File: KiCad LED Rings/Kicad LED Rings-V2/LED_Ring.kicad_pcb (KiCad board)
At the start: 4 copper layers, 30 x 30 mm, 28 parts, among them J1 Conn_01x02_Female, J2 Conn_01x02_Male, U1 LM3509SD_NOPB

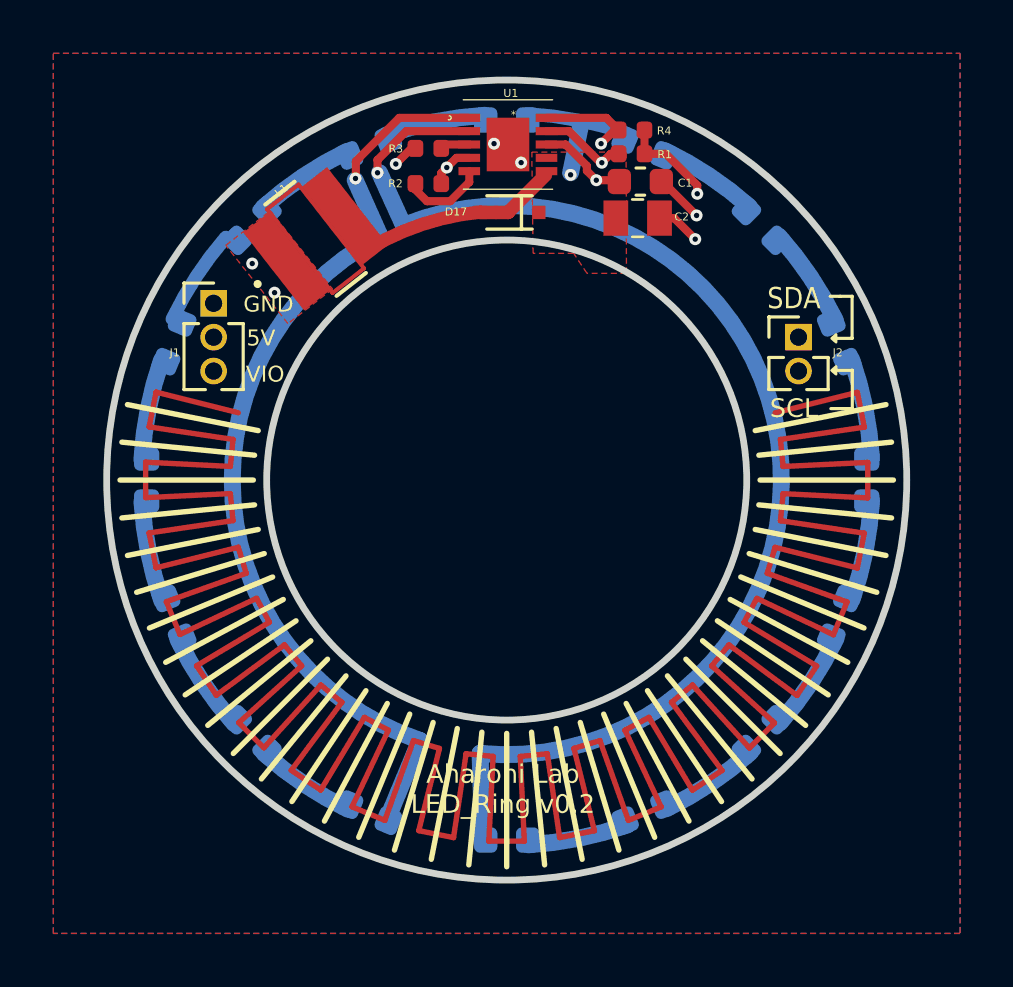
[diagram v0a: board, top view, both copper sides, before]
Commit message: Modified PCB layout
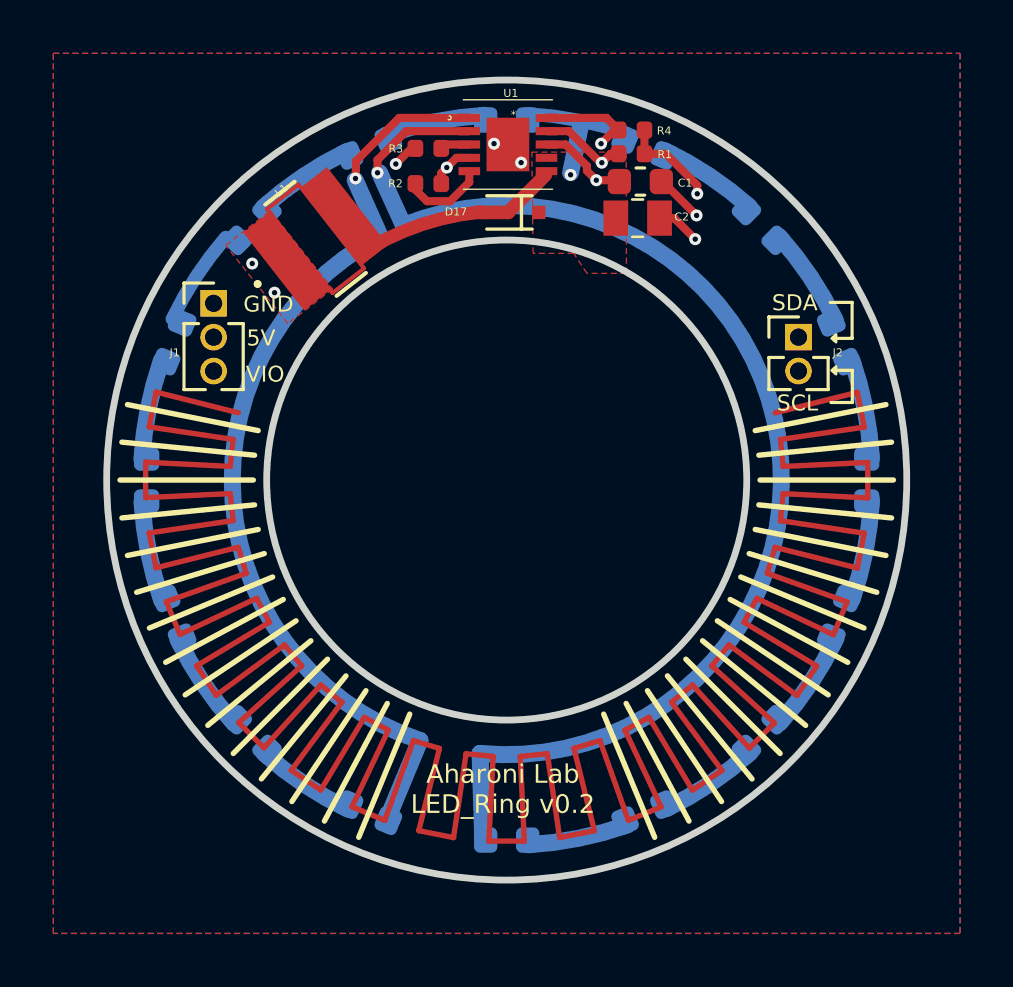
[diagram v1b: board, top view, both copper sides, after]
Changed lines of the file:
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@@
   (general
     (thickness 1.6)
-    (drawings 166)
+    (drawings 159)
     (tracks 105)
     (zones 0)
@@
   (gr_line (start 115.277917 87.898961) (end 118.055768 92.056309) (layer F.SilkS) (width 0.203))
   (gr_line (start 113.635493 88.776856) (end 115.54891 93.396254) (layer F.SilkS) (width 0.203))
-  (gr_line (start 111.853358 89.31746) (end 112.82881 94.221386) (layer F.SilkS) (width 0.203))
-  (gr_line (start 110 89.5) (end 110 94.5) (layer F.SilkS) (width 0.203))
-  (gr_line (start 108.146642 89.31746) (end 107.17119 94.221386) (layer F.SilkS) (width 0.203))
   (gr_line (start 106.364507 88.776856) (end 104.45109 93.396254) (layer F.SilkS) (width 0.203))
   (gr_line (start 104.722083 87.898961) (end 101.944232 92.056309) (layer F.SilkS) (width 0.203))
@@
   (gr_line (start 116.026736 87.343599) (end 119.198703 91.208651) (layer F.SilkS) (width 0.203))
   (gr_line (start 114.478269 88.378252) (end 116.835253 92.787859) (layer F.SilkS) (width 0.203))
-  (gr_line (start 112.757705 89.090933) (end 114.209129 93.875635) (layer F.SilkS) (width 0.203))
-  (gr_line (start 110.931163 89.454255) (end 111.421249 94.430179) (layer F.SilkS) (width 0.203))
-  (gr_line (start 109.068837 89.454255) (end 108.578752 94.430179) (layer F.SilkS) (width 0.203))
-  (gr_line (start 107.242296 89.090933) (end 105.790873 93.875635) (layer F.SilkS) (width 0.203))
   (gr_line (start 105.521731 88.378252) (end 103.164747 92.787859) (layer F.SilkS) (width 0.203))
   (gr_line (start 103.973264 87.343599) (end 100.801298 91.208652) (layer F.SilkS) (width 0.203))
@@
   (gr_arc (start 110 80) (end 105.2576 70.866) (angle -134.1265598) (layer B.Cu) (width 0.635))
   (gr_arc (start 110 80) (end 109 90.25) (angle -207.5661477) (layer B.Cu) (width 0.635))
-  (gr_line (start 122.4986 73.10992) (end 122.1303 73.10992) (layer F.SilkS) (width 0.12))
-  (gr_line (start 122.56464 77.32124) (end 122.15316 77.32124) (layer F.SilkS) (width 0.12))
+  (gr_line (start 122.4986 73.33852) (end 122.1303 73.33852) (layer F.SilkS) (width 0.12))
+  (gr_line (start 122.56464 77.09264) (end 122.15316 77.09264) (layer F.SilkS) (width 0.12))
   (gr_poly (pts (xy 122.35128 75.88868) (xy 122.35128 75.74136) (xy 122.18364 75.88868) (xy 122.35128 76.03346)) (layer F.SilkS) (width 0.1))
   (gr_poly (pts (xy 122.35128 74.68726) (xy 122.35128 74.53994) (xy 122.18364 74.68726) (xy 122.35128 74.83204)) (layer F.SilkS) (width 0.1))
   (gr_line (start 122.95834 75.88614) (end 122.3081 75.88614) (layer F.SilkS) (width 0.12))
-  (gr_line (start 122.95834 77.32124) (end 122.95834 75.88614) (layer F.SilkS) (width 0.12))
-  (gr_line (start 122.56464 77.32124) (end 122.95834 77.32124) (layer F.SilkS) (width 0.12))
+  (gr_line (start 122.95834 77.09264) (end 122.95834 75.88614) (layer F.SilkS) (width 0.12))
+  (gr_line (start 122.56464 77.09264) (end 122.95834 77.09264) (layer F.SilkS) (width 0.12))
   (gr_line (start 122.95072 74.68726) (end 122.33096 74.68726) (layer F.SilkS) (width 0.12))
-  (gr_line (start 122.95072 73.10992) (end 122.95072 74.68726) (layer F.SilkS) (width 0.12))
-  (gr_line (start 122.4986 73.10992) (end 122.95072 73.10992) (layer F.SilkS) (width 0.12))
-  (gr_text SCL (at 120.7714 77.31108) (layer F.SilkS)
-    (effects (font (size 0.7 0.7) (thickness 0.15)))
-  )
-  (gr_text SDA (at 120.7714 73.18866) (layer F.SilkS)
-    (effects (font (size 0.8 0.7) (thickness 0.15)))
+  (gr_line (start 122.95072 73.33852) (end 122.95072 74.68726) (layer F.SilkS) (width 0.12))
+  (gr_line (start 122.4986 73.33852) (end 122.95072 73.33852) (layer F.SilkS) (width 0.12))
+  (gr_text SCL (at 120.904 77.1144) (layer F.SilkS)
+    (effects (font (size 0.6 0.6) (thickness 0.1)))
+  )
+  (gr_text SDA (at 120.8024 73.3552) (layer F.SilkS)
+    (effects (font (size 0.6 0.6) (thickness 0.1)))
   )
   (gr_text VIO (at 100.94162 76.03346) (layer F.SilkS)
